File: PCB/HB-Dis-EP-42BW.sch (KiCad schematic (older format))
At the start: 20 parts, among them J1 Reset, J2 FTDI, J3 Conn_01x04, J4 ePaper, J5 Buttons, SW1 SW_Push, U1 ATMEGA1284P-AU, U2 CC1101

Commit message: lots of changes
- TH buttons
- footprint of ePaper
- footprint of adapter board
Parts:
- removed J5: Buttons, symbol Conn_02x10_Row_Letter_Last
- added J6: Supply, Pin_Headers:Pin_Header_Straight_1x02_Pitch2.54mm, symbol Conn_01x02
- added SW1, SW10, SW2, SW3, SW4, SW5, SW6, SW7, SW8, SW9: SW_Push, Buttons_Switches_THT:SW_PUSH_6mm, symbol SW_Push
- D1: renamed from D?; footprint (none) -> LEDs:LED_D3.0mm-3
- J4: footprint (none) -> CFA-10084:CFA-10084
- R2, R3: footprint (none) -> Resistors_SMD:R_0603_HandSoldering
- SW0: renamed from SW1; footprint (none) -> Buttons_Switches_THT:SW_PUSH_6mm
- U1: footprint TQFP44 -> Housings_QFP:TQFP-44_10x10mm_Pitch0.8mm
- U2: footprint CC1101_Module:CC1101_SMD -> CC1101_module:CC1101_Module
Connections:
- wire segments 115 -> 122
- no-connect marks 16 -> 14
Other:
- moved on the sheet: C8

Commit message: initial PCB placement
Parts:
- removed D1: LED_Dual_AAC, LEDs:LED_D3.0mm-3, symbol LED_Dual_AAC
- added D1: LED_Dual, LEDs:LED_D3.0mm-3, symbol LED_Dual_ACA
- J3: value Conn_01x04 -> Conn_ISP
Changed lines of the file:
@@
 P 1125 6075
 F 0 "J3" H 1125 6275 50  0000 C CNN
-F 1 "Conn_01x04" H 1125 5775 50  0000 C CNN
+F 1 "Conn_ISP" H 1125 5775 50  0000 C CNN
 F 2 "Pin_Headers:Pin_Header_Straight_1x04_Pitch2.54mm" H 1125 6075 50  0001 C CNN
 F 3 "" H 1125 6075 50  0001 C CNN
@@
 NoConn ~ 9800 2525
 $Comp
-L LED_Dual_AAC D1
-U 1 1 5C0CE5F6
-P 5350 6500
-F 0 "D1" H 5350 6725 50  0000 C CNN
-F 1 "LED_Dual_AAC" H 5350 6250 50  0000 C CNN
-F 2 "LEDs:LED_D3.0mm-3" H 5350 6500 50  0001 C CNN
-F 3 "" H 5350 6500 50  0001 C CNN
-	1    5350 6500
-	-1   0    0    1
-$EndComp
-$Comp
 L GND #PWR019
 U 1 1 5C0CE96D
@@
 	4400 6400 4650 6400
 Text Label 4400 6400 0    60   ~ 0
+LED1
+Text Label 4400 6600 0    60   ~ 0
 LED2
-Text Label 4400 6600 0    60   ~ 0
-LED1
 $Comp
 L SW_Push SW0
@@
 	8900 6300 9025 6300
 Connection ~ 9025 6300
+$Comp
+L LED_Dual_ACA D1
+U 1 1 5C157081
+P 5350 6500
+F 0 "D1" H 5350 6725 50  0000 C CNN
+F 1 "LED_Dual" H 5350 6250 50  0000 C CNN
+F 2 "LEDs:LED_D3.0mm-3" H 5350 6500 50  0001 C CNN
+F 3 "" H 5350 6500 50  0001 C CNN
+	1    5350 6500
+	-1   0    0    -1
+$EndComp
 $EndSCHEMATC

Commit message: first board layout done, buttons swapped
buttons are connected differently to simplify routing
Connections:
- net BTN1: now also U1.37 ((PCINT0/ADC0)PA0); no longer U1.30 ((PCINT7/ADC7)PA7)
- net BTN10: now also U1.25 ((PCINT22/TOSC1)PC6); no longer U1.26 ((PCINT23/TOSC2)PC7)
- net BTN2: now also U1.36 ((PCINT1/ADC1)PA1); no longer U1.31 ((PCINT6/ADC6)PA6)
- net BTN3: now also U1.35 ((PCINT2/ADC2)PA2); no longer U1.32 ((PCINT5/ADC5)PA5)
- net BTN4: now also U1.34 ((PCINT3/ADC3)PA3); no longer U1.33 ((PCINT4/ADC4)PA4)
- net BTN5: now also U1.33 ((PCINT4/ADC4)PA4); no longer U1.34 ((PCINT3/ADC3)PA3)
- net BTN6: now also U1.32 ((PCINT5/ADC5)PA5); no longer U1.35 ((PCINT2/ADC2)PA2)
- net BTN7: now also U1.31 ((PCINT6/ADC6)PA6); no longer U1.36 ((PCINT1/ADC1)PA1)
- net BTN8: now also U1.30 ((PCINT7/ADC7)PA7); no longer U1.37 ((PCINT0/ADC0)PA0)
- net BTN9: now also U1.26 ((PCINT23/TOSC2)PC7); no longer U1.25 ((PCINT22/TOSC1)PC6)
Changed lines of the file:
@@
 	6150 3950 6550 3950
 Text Label 6550 2150 2    60   ~ 0
+BTN8
+Text Label 6550 2050 2    60   ~ 0
+BTN7
+Text Label 6550 1950 2    60   ~ 0
+BTN6
+Text Label 6550 1850 2    60   ~ 0
+BTN5
+Text Label 6550 1750 2    60   ~ 0
+BTN4
+Text Label 6550 1650 2    60   ~ 0
+BTN3
+Text Label 6550 1550 2    60   ~ 0
+BTN2
+Text Label 6550 1450 2    60   ~ 0
 BTN1
-Text Label 6550 2050 2    60   ~ 0
-BTN2
-Text Label 6550 1950 2    60   ~ 0
-BTN3
-Text Label 6550 1850 2    60   ~ 0
-BTN4
-Text Label 6550 1750 2    60   ~ 0
-BTN5
-Text Label 6550 1650 2    60   ~ 0
-BTN6
-Text Label 6550 1550 2    60   ~ 0
-BTN7
-Text Label 6550 1450 2    60   ~ 0
-BTN8
 Text Label 6550 3850 2    60   ~ 0
+BTN10
+Text Label 6550 3950 2    60   ~ 0
 BTN9
-Text Label 6550 3950 2    60   ~ 0
-BTN10
 Text Label 6550 2350 2    60   ~ 0
 LED1

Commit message: added opt. 8 MHz resonator
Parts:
- added R4: 1M, Resistors_SMD:R_0603_HandSoldering, symbol R
- added Y1: Resonator, Resonators:Resonator_SMD_muRata_TPSKA-3pin_7.9x3.8mm_HandSoldering, symbol Resonator
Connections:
- net GND: now also Y1.2
- net at U1.7 (XTAL2): now also R4.1, Y1.1
- net at U1.8 (XTAL1): now also R4.2, Y1.3
- no-connect marks 14 -> 12
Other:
- note added: "Dec. 2018"
- note removed: "Oct. 2018"
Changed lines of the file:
@@
 License: CC BY-NC-SA 3.0
 Text Notes 8150 7650 0    60   ~ 0
-Oct. 2018
+Dec. 2018
 Text Label 8500 2625 0    60   ~ 0
 GDO0
@@
 NoConn ~ 6150 4350
 NoConn ~ 6150 4650
-NoConn ~ 4150 2250
-NoConn ~ 4150 1850
 $Comp
 L Conn_01x08 J4
@@
 	-1   0    0    -1
 $EndComp
+$Comp
+L Resonator Y1
+U 1 1 5C16C97D
+P 3825 2050
+F 0 "Y1" H 3825 2275 50  0000 C CNN
+F 1 "Resonator" H 3825 2200 50  0000 C CNN
+F 2 "Resonators:Resonator_SMD_muRata_TPSKA-3pin_7.9x3.8mm_HandSoldering" H 3800 2050 50  0001 C CNN
+F 3 "" H 3800 2050 50  0001 C CNN
+	1    3825 2050
+	0    1    1    0
+$EndComp
+Wire Wire Line
+	3400 2250 4150 2250
+Wire Wire Line
+	3825 2250 3825 2200
+Wire Wire Line
+	3400 1850 4150 1850
+Wire Wire Line
+	3825 1850 3825 1900
+$Comp
+L R R4
+U 1 1 5C16CD7A
+P 3400 2050
+F 0 "R4" V 3480 2050 50  0000 C CNN
+F 1 "1M" V 3400 2050 50  0000 C CNN
+F 2 "Resistors_SMD:R_0603_HandSoldering" V 3330 2050 50  0001 C CNN
+F 3 "" H 3400 2050 50  0001 C CNN
+	1    3400 2050
+	1    0    0    -1
+$EndComp
+$Comp
+L GND #PWR025
+U 1 1 5C16CF92
+P 3575 2350
+F 0 "#PWR025" H 3575 2100 50  0001 C CNN
+F 1 "GND" H 3575 2200 50  0000 C CNN
+F 2 "" H 3575 2350 50  0001 C CNN
+F 3 "" H 3575 2350 50  0001 C CNN
+	1    3575 2350
+	1    0    0    -1
+$EndComp
+Wire Wire Line
+	3400 1850 3400 1900
+Connection ~ 3825 1850
+Wire Wire Line
+	3400 2200 3400 2250
+Connection ~ 3825 2250
+Wire Wire Line
+	3625 2050 3575 2050
+Wire Wire Line
+	3575 2050 3575 2350
 $EndSCHEMATC

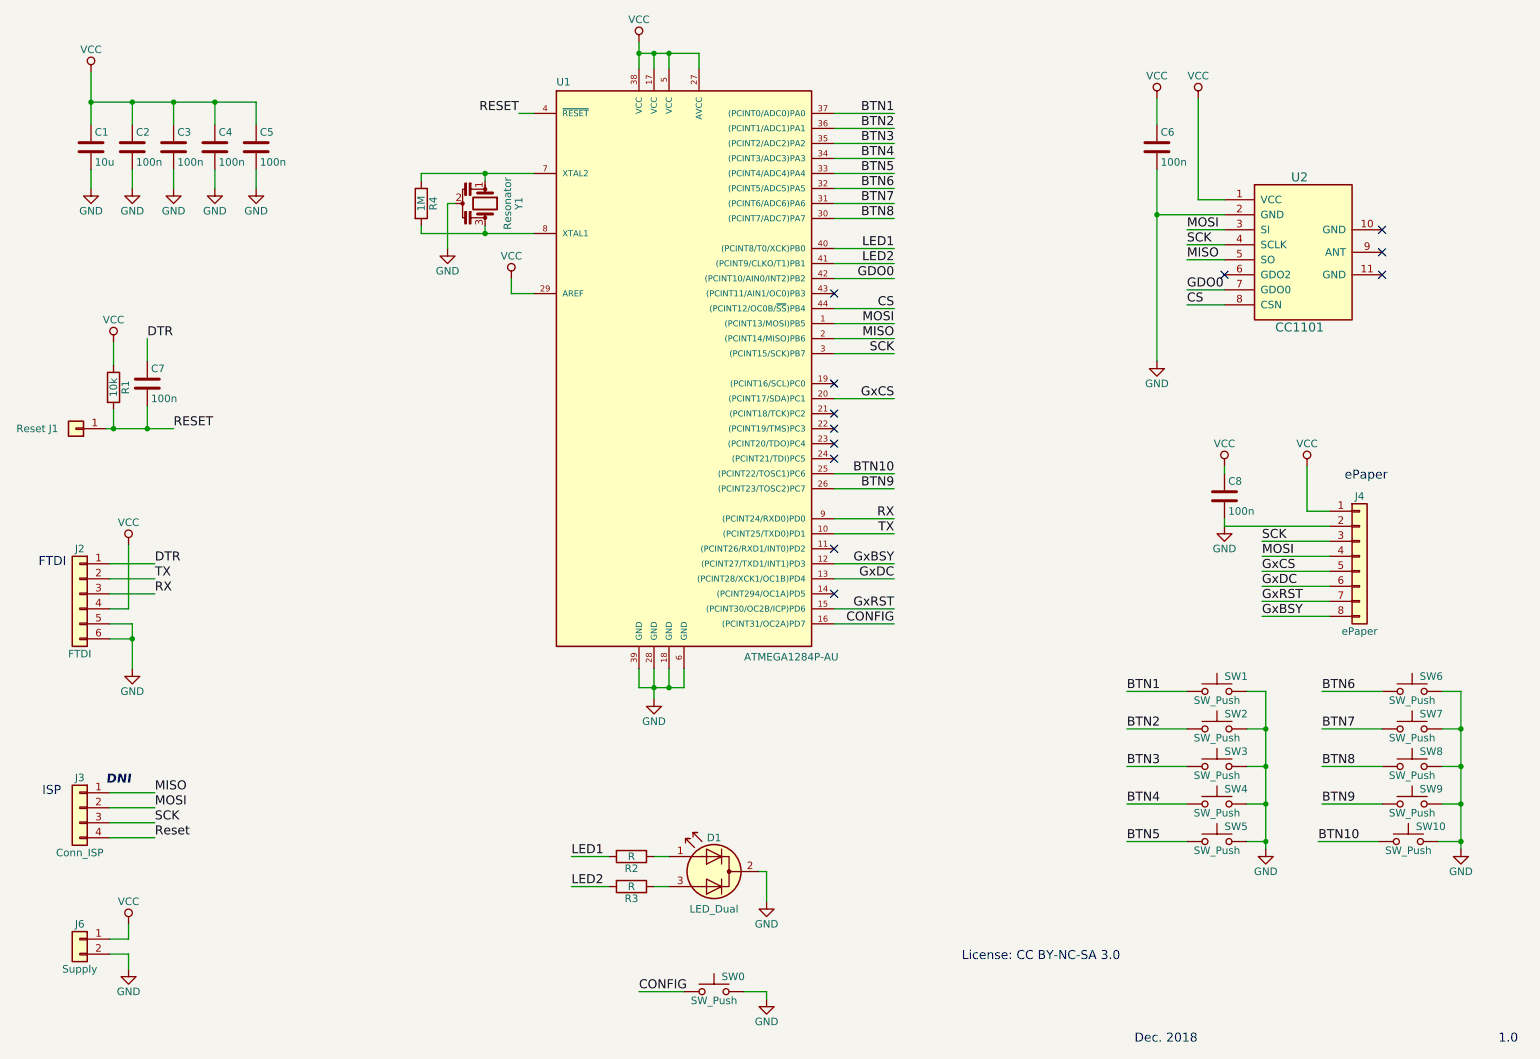
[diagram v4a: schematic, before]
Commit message: replace bare ePaper by module
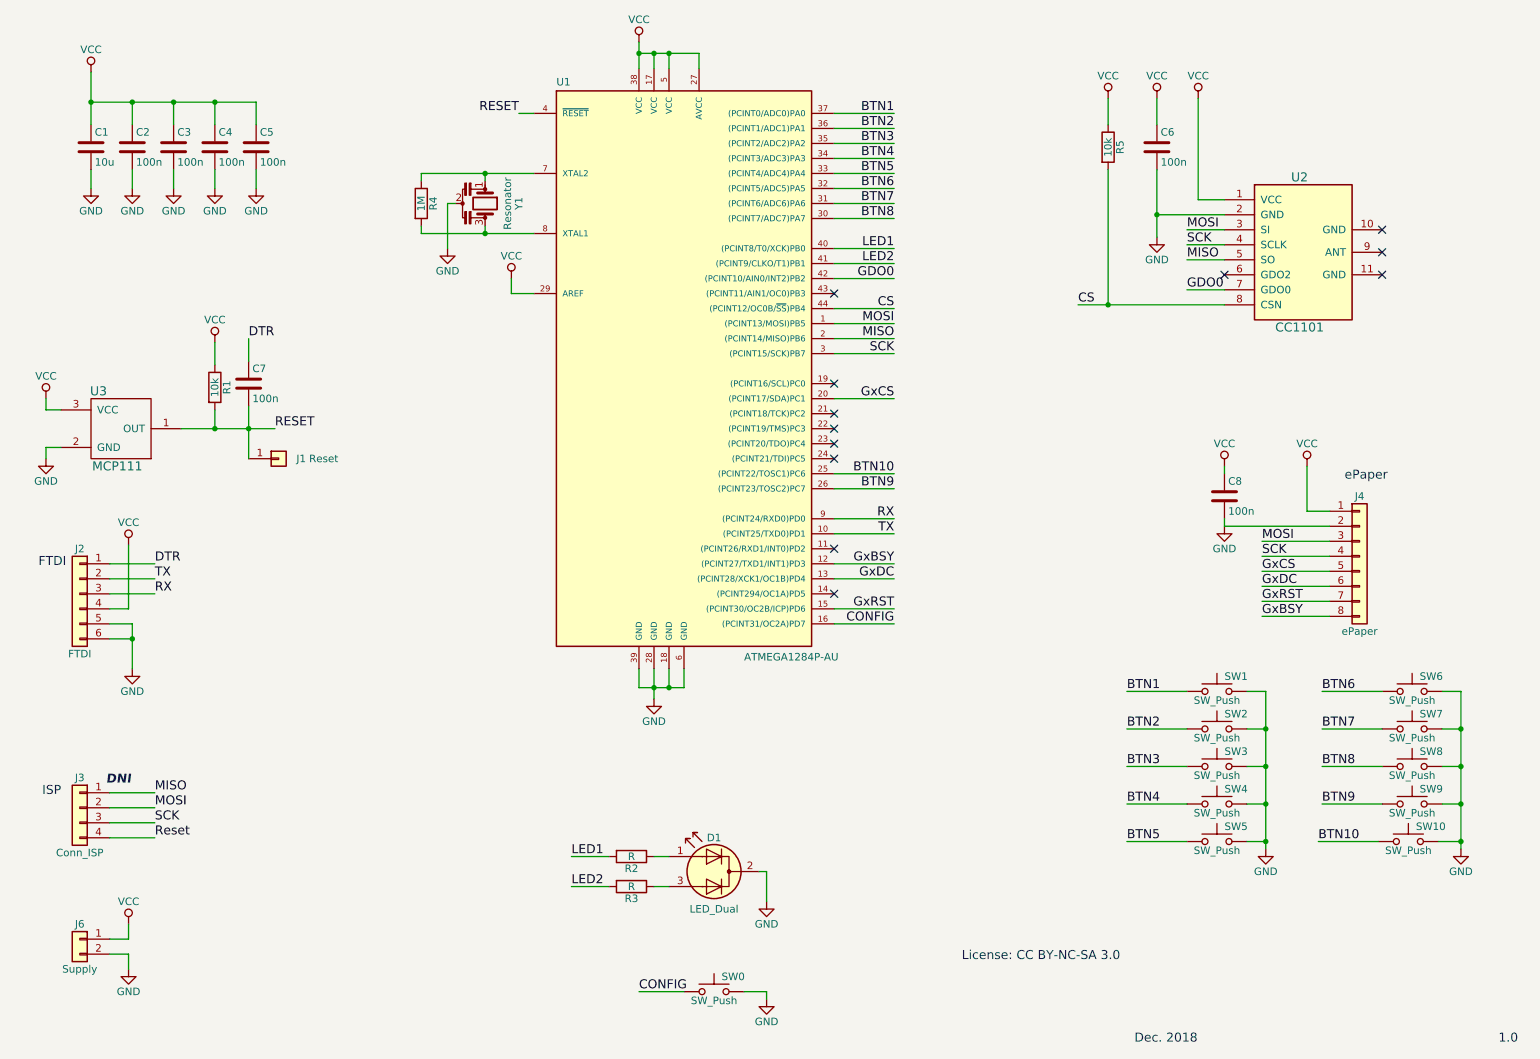
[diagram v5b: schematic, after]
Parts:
- added R5: 10k, Resistors_SMD:R_0603_HandSoldering, symbol R
- added U3: MCP111, TO_SOT_Packages_SMD:SOT-23, symbol MCP111
- J4: footprint CFA-10084:CFA-10084 -> Waveshare_ePaper:Waveshare_4.2inch_Module
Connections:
- net CS: now also R5.2
- net GND: now also U3.2 (GND)
- net MOSI: now also J4.3 (Pin_3); no longer J4.4 (Pin_4)
- net RESET: now also U3.1 (OUT)
- net SCK: now also J4.4 (Pin_4); no longer J4.3 (Pin_3)
- net VCC: now also R5.1, U3.3 (VCC)
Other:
- moved on the sheet: C7, J1, R1
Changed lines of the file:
@@
 LIBS:valves
 LIBS:cc1101-module
+LIBS:mcp111
 LIBS:HB-Dis-EP-42BW-cache
 EELAYER 25 0
@@
 L R R1
 U 1 1 5AD3185F
-P 1350 3275
-F 0 "R1" V 1430 3275 50  0000 C CNN
-F 1 "10k" V 1350 3275 50  0000 C CNN
-F 2 "Resistors_SMD:R_0603_HandSoldering" V 1280 3275 50  0001 C CNN
-F 3 "" H 1350 3275 50  0001 C CNN
-	1    1350 3275
+P 2025 3275
+F 0 "R1" V 2105 3275 50  0000 C CNN
+F 1 "10k" V 2025 3275 50  0000 C CNN
+F 2 "Resistors_SMD:R_0603_HandSoldering" V 1955 3275 50  0001 C CNN
+F 3 "" H 2025 3275 50  0001 C CNN
+	1    2025 3275
 	1    0    0    -1
 $EndComp
@@
 L VCC #PWR01
 U 1 1 5AD31983
-P 1350 2975
-F 0 "#PWR01" H 1350 2825 50  0001 C CNN
-F 1 "VCC" H 1350 3125 50  0000 C CNN
-F 2 "" H 1350 2975 50  0001 C CNN
-F 3 "" H 1350 2975 50  0001 C CNN
-	1    1350 2975
+P 900 3350
+F 0 "#PWR01" H 900 3200 50  0001 C CNN
+F 1 "VCC" H 900 3500 50  0000 C CNN
+F 2 "" H 900 3350 50  0001 C CNN
+F 3 "" H 900 3350 50  0001 C CNN
+	1    900  3350
 	1    0    0    -1
 $EndComp
@@
 L GND #PWR02
 U 1 1 5AD31F67
-P 8300 3100
-F 0 "#PWR02" H 8300 2850 50  0001 C CNN
-F 1 "GND" H 8300 2950 50  0000 C CNN
-F 2 "" H 8300 3100 50  0001 C CNN
-F 3 "" H 8300 3100 50  0001 C CNN
-	1    8300 3100
+P 8300 2275
+F 0 "#PWR02" H 8300 2025 50  0001 C CNN
+F 1 "GND" H 8300 2125 50  0000 C CNN
+F 2 "" H 8300 2275 50  0001 C CNN
+F 3 "" H 8300 2275 50  0001 C CNN
+	1    8300 2275
 	1    0    0    -1
 $EndComp
@@
 L C C7
 U 1 1 5AD3532A
-P 1575 3250
-F 0 "C7" H 1600 3350 50  0000 L CNN
-F 1 "100n" H 1600 3150 50  0000 L CNN
-F 2 "Capacitors_SMD:C_0603_HandSoldering" H 1613 3100 50  0001 C CNN
-F 3 "" H 1575 3250 50  0001 C CNN
-	1    1575 3250
-	1    0    0    -1
-$EndComp
-Text Label 1575 2950 0    60   ~ 0
+P 2250 3250
+F 0 "C7" H 2275 3350 50  0000 L CNN
+F 1 "100n" H 2275 3150 50  0000 L CNN
+F 2 "Capacitors_SMD:C_0603_HandSoldering" H 2288 3100 50  0001 C CNN
+F 3 "" H 2250 3250 50  0001 C CNN
+	1    2250 3250
+	1    0    0    -1
+$EndComp
+Text Label 2250 2950 0    60   ~ 0
 DTR
 $Comp
@@
 L Conn_01x01 J1
 U 1 1 5B4BEEED
-P 1100 3550
-F 0 "J1" H 1250 3550 50  0000 C CNN
-F 1 "Reset" H 1400 3550 50  0000 C CNN
-F 2 "Testpads:Testpad" H 1100 3550 50  0001 C CNN
-F 3 "" H 1100 3550 50  0001 C CNN
-	1    1100 3550
-	-1   0    0    1
+P 2450 3750
+F 0 "J1" H 2600 3750 50  0000 C CNN
+F 1 "Reset" H 2750 3750 50  0000 C CNN
+F 2 "Testpads:Testpad" H 2450 3750 50  0001 C CNN
+F 3 "" H 2450 3750 50  0001 C CNN
+	1    2450 3750
+	1    0    0    -1
 $EndComp
 Text Notes 10575 7650 0    60   ~ 0
@@
 $EndComp
 Wire Wire Line
-	1350 2975 1350 3125
+	2025 2975 2025 3125
 Wire Wire Line
 	8300 1350 8300 1525
@@
 	8575 2025 8750 2025
 Wire Wire Line
-	8300 1825 8300 3100
+	8300 1825 8300 2275
 Wire Wire Line
 	8300 2125 8750 2125
@@
 	4000 2650 4000 2550
 Wire Wire Line
-	1350 3425 1350 3550
-Wire Wire Line
-	1300 3550 1750 3550
-Connection ~ 1350 3550
-Wire Wire Line
-	1575 3100 1575 2950
-Wire Wire Line
-	1575 3550 1575 3400
-Connection ~ 1575 3550
-Text Label 1750 3550 0    60   ~ 0
+	2025 3425 2025 3550
+Wire Wire Line
+	1800 3550 2425 3550
+Connection ~ 2025 3550
+Wire Wire Line
+	2250 3100 2250 2950
+Wire Wire Line
+	2250 3400 2250 3750
+Connection ~ 2250 3550
+Text Label 2425 3550 0    60   ~ 0
 RESET
 Wire Wire Line
@@
 Wire Wire Line
 	8500 2625 8750 2625
-Wire Wire Line
-	8500 2725 8750 2725
 Text Label 8500 2225 0    60   ~ 0
 MOSI
@@
 Text Label 8500 2425 0    60   ~ 0
 MISO
-Text Label 8500 2725 0    60   ~ 0
+Text Label 7775 2725 0    60   ~ 0
 CS
 Text Label 6550 2750 2    60   ~ 0
@@
 F 0 "J4" H 9650 4800 50  0000 C CNN
 F 1 "ePaper" H 9650 3900 50  0000 C CNN
-F 2 "CFA-10084:CFA-10084" H 9650 4400 50  0001 C CNN
+F 2 "Waveshare_ePaper:Waveshare_4.2inch_Module" H 9650 4400 50  0001 C CNN
 F 3 "" H 9650 4400 50  0001 C CNN
 	1    9650 4400
@@
 	9000 4300 9450 4300
 Text Label 9000 4300 0    60   ~ 0
+MOSI
+Text Label 9000 4400 0    60   ~ 0
 SCK
-Text Label 9000 4400 0    60   ~ 0
-MOSI
 $Comp
 L SW_Push SW1
@@
 Wire Wire Line
 	3575 2050 3575 2350
+$Comp
+L R R5
+U 1 1 5C1A72D8
+P 7975 1675
+F 0 "R5" V 8055 1675 50  0000 C CNN
+F 1 "10k" V 7975 1675 50  0000 C CNN
+F 2 "Resistors_SMD:R_0603_HandSoldering" V 7905 1675 50  0001 C CNN
+F 3 "" H 7975 1675 50  0001 C CNN
+	1    7975 1675
+	1    0    0    -1
+$EndComp
+Wire Wire Line
+	7975 1825 7975 2725
+Connection ~ 7975 2725
+Wire Wire Line
+	7775 2725 8750 2725
+$Comp
+L VCC #PWR026
+U 1 1 5C1A7BAD
+P 7975 1350
+F 0 "#PWR026" H 7975 1200 50  0001 C CNN
+F 1 "VCC" H 7975 1500 50  0000 C CNN
+F 2 "" H 7975 1350 50  0001 C CNN
+F 3 "" H 7975 1350 50  0001 C CNN
+	1    7975 1350
+	1    0    0    -1
+$EndComp
+Wire Wire Line
+	7975 1525 7975 1350
+$Comp
+L MCP111 U3
+U 1 1 5C1A7F16
+P 1400 3550
+F 0 "U3" H 1250 3800 60  0000 C CNN
+F 1 "MCP111" H 1375 3300 60  0000 C CNN
+F 2 "TO_SOT_Packages_SMD:SOT-23" H 1400 3550 60  0001 C CNN
+F 3 "" H 1400 3550 60  0001 C CNN
+	1    1400 3550
+	1    0    0    -1
+$EndComp
+$Comp
+L GND #PWR027
+U 1 1 5C1A845B
+P 900 3750
+F 0 "#PWR027" H 900 3500 50  0001 C CNN
+F 1 "GND" H 900 3600 50  0000 C CNN
+F 2 "" H 900 3750 50  0001 C CNN
+F 3 "" H 900 3750 50  0001 C CNN
+	1    900  3750
+	1    0    0    -1
+$EndComp
+Wire Wire Line
+	900  3750 900  3675
+Wire Wire Line
+	900  3675 1000 3675
+Wire Wire Line
+	900  3350 900  3425
+Wire Wire Line
+	900  3425 1000 3425
+$Comp
+L VCC #PWR028
+U 1 1 5C1A87C4
+P 2025 2975
+F 0 "#PWR028" H 2025 2825 50  0001 C CNN
+F 1 "VCC" H 2025 3125 50  0000 C CNN
+F 2 "" H 2025 2975 50  0001 C CNN
+F 3 "" H 2025 2975 50  0001 C CNN
+	1    2025 2975
+	1    0    0    -1
+$EndComp
 $EndSCHEMATC
